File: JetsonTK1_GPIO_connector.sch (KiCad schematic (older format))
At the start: 35 parts

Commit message: アートワーク開始
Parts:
- removed P?: CONN_02X08, symbol CONN_02X08
- added JP2, JP3, JP6: Jumper_NC_Dual, Connect:GS3, symbol Jumper_NC_Dual
- added P4: CONN_01X01, Pin_Headers:Pin_Header_Straight_1x01, symbol CONN_01X01
- added P5, P6: CONN_01X04, Pin_Headers:Pin_Header_Straight_1x04, symbol CONN_01X04
- added P9: CONN_02X10, Pin_Headers:Pin_Header_Straight_2x10, symbol CONN_02X10
- added R10, R11, R13, R15, R17, R3, R4, R5, R6, R7, R8, R9: R, Resistors_SMD:R_0603, symbol R
- C1, C2, C3, C4, C5: renamed from C?; footprint (none) -> Capacitors_SMD:C_0603
- D1, D2, D3, D4: renamed from D?; footprint (none) -> LEDs:LED_0603
- JP1, JP4, JP5, JP7, JP8: renamed from JP?; footprint (none) -> Connect:GS3
- P1: renamed from P?; footprint (none) -> Pin_Headers:Pin_Header_Straight_1x25_Pitch2.00mm
- P10: renamed from P?; footprint (none) -> Pin_Headers:Pin_Header_Straight_1x10
- P2, P3: renamed from P?; footprint (none) -> Pin_Headers:Pin_Header_Straight_2x25_Pitch2.00mm
- P7, P8: renamed from P?; footprint (none) -> Pin_Headers:Pin_Header_Straight_1x04
- R1, R12, R14, R16, R18, R19, R2, R20, R21, R22, R23: renamed from R?; footprint (none) -> Resistors_SMD:R_0603
- gave numbers to parts that had none: 3
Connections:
- net +12V: now also P3.26 (P26); no longer P3.25 (P25)
- net +1V8: now also P3.20 (P20), P3.4 (P4), R11.1, R13.1, R3.1, R4.1, R5.1, R6.1; no longer C4.2, JP4.3, JP5.3, JP7.3, P3.19 (P19), P3.3 (P3), U2.24 (VDD)
- net +3V3: now also P3.15 (P15), JP2.1, JP3.1, JP6.1; no longer P3.16 (P16)
- net +5V: now also P2.2 (P2), P3.2 (P2), JP2.3, JP3.3, JP6.3; no longer P2.1 (P1), P3.1 (P1)
- net CAM_I2C_SCL: now also P2.7 (P7), R11.2; no longer P2.8 (P8)
- net CAM_I2C_SDA: now also P2.5 (P5), R13.2; no longer P2.6 (P6)
- net GEN1_I2C_SCL: now also P2.37 (P37), R3.2; no longer P2.38 (P38)
- net GEN1_I2C_SDA: now also P2.39 (P39), R5.2; no longer P2.40 (P40)
- net GND: now also P2.14 (P14), P2.15 (P15), P2.21 (P21), P2.25 (P25), P2.31 (P31), P2.41 (P41), P2.50 (P50), P2.8 (P8), P2.9 (P9), P3.1 (P1), P3.10 (P10), P3.13 (P13), P3.16 (P16), P3.25 (P25), P3.30 (P30), P3.31 (P31), P3.36 (P36), P3.37 (P37), P3.42 (P42), P3.43 (P43), P3.48 (P48), P3.7 (P7), P5.4 (P4), P6.4 (P4), P9.19 (P19), P9.20 (P20); no longer P2.10 (P10), P2.13 (P13), P2.16 (P16), P2.22 (P22), P2.26 (P26), P2.32 (P32), P2.42 (P42), P2.49 (P49), P2.7 (P7), P3.14 (P14), P3.15 (P15), P3.2 (P2), P3.26 (P26), P3.29 (P29), P3.32 (P32), P3.35 (P35), P3.38 (P38), P3.41 (P41), P3.44 (P44), P3.47 (P47), P3.8 (P8), P3.9 (P9)
- net GPIO_PH1: now also P3.49 (P49); no longer P3.50 (P50)
- net GPIO_PK2: now also P3.18 (P18); no longer P3.17 (P17)
- net GPIO_PU0: now also P2.28 (P28); no longer P2.27 (P27)
- net GPIO_PU1: now also P2.30 (P30); no longer P2.29 (P29)
- net GPIO_PU2: now also P2.32 (P32); no longer P2.31 (P31)
- net GPIO_PU3: now also P2.34 (P34); no longer P2.33 (P33)
- net GPIO_PU4: now also P2.36 (P36); no longer P2.35 (P35)
- net GPIO_PU5: now also P2.38 (P38); no longer P2.37 (P37)
- net GPIO_PU6: now also P2.40 (P40); no longer P2.39 (P39)
- net I2C_SCL_1V8: now also P3.22 (P22); no longer P3.21 (P21)
- net I2C_SCL_3V3: now also P3.17 (P17); no longer P3.18 (P18)
- net I2C_SDA_1V8: now also P3.24 (P24); no longer P3.23 (P23)
- net I2C_SDA_3V3: now also P3.19 (P19); no longer P3.20 (P20)
- net PWR_I2C_SCL: now also P2.33 (P33), R4.2; no longer P2.34 (P34)
- net PWR_I2C_SDA: now also P2.35 (P35), R6.2; no longer P2.36 (P36)
- net TS_SPI_CS_L: now also P3.5 (P5); no longer P3.6 (P6)
- net TS_SPI_MISO: now also P3.8 (P8); no longer P3.7 (P7)
- net TS_SPI_MOSI: now also P3.6 (P6); no longer P3.5 (P5)
- net TS_SPI_SCK: now also P3.3 (P3); no longer P3.4 (P4)
- net logic_conv_1/HV1: now also P5.2 (P2), R7.2
- net logic_conv_1/HV2: now also P5.3 (P3), R9.2
- net logic_conv_1/VH: now also JP2.2, P5.1 (P1), R7.1, R9.1
- net logic_conv_2/HV1: now also P6.2 (P2), R8.2
- net logic_conv_2/HV2: now also P6.3 (P3), R10.2
- net logic_conv_2/VH: now also JP3.2, P6.1 (P1), R10.1, R8.1
- net at U2.1 (~INT): now also P4.1 (P1)
- net at U2.10 (P0_6): now also P9.6 (P6)
- net at U2.11 (P0_7): now also P9.4 (P4)
- net at U2.13 (P1_0): now also P9.17 (P17)
- net at U2.14 (P1_1): now also P9.15 (P15)
- net at U2.15 (P1_2): now also P9.13 (P13)
- net at U2.16 (P1_3): now also P9.11 (P11)
- net at U2.17 (P1_4): now also P9.9 (P9)
- net at U2.18 (P1_5): now also P9.7 (P7)
- net at U2.19 (P1_6): now also P9.5 (P5)
- net at U2.20 (P1_7): now also P9.3 (P3)
- net logic_conv_3/HV1: now reaches U2.22 (SCL)
- net logic_conv_3/HV1: now also R15.2
- net logic_conv_3/HV2: now reaches U2.23 (SDA)
- net logic_conv_3/HV2: now also R17.2
- net at U2.4 (P0_0): now also P9.18 (P18)
- net at U2.5 (P0_1): now also P9.16 (P16)
- net at U2.6 (P0_2): now also P9.14 (P14)
- net at U2.7 (P0_3): now also P9.12 (P12)
- net at U2.8 (P0_4): now also P9.10 (P10)
- net at U2.9 (P0_5): now also P9.8 (P8)
- new net logic_conv_3/VH: C4.2, JP4.3, JP5.3, JP6.2, JP7.3, P9.1 (P1), P9.2 (P2), R15.1, R17.1, U2.24 (VDD)
- no-connect marks 2 -> 74
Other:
- moved on the sheet: C4, JP4, JP5, JP7, P8, R18, R19, U2

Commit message: 進捗
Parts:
- removed R10, R11, R13, R15, R17, R3, R4, R5, R6, R7, R8, R9: R, Resistors_SMD:R_0603, symbol R
- P10: footprint Pin_Headers:Pin_Header_Straight_1x10 -> Connectors_JST:JST_XH_B10B-XH-A_10x2.50mm_Straight
- P5, P6, P7, P8: footprint Pin_Headers:Pin_Header_Straight_1x04 -> Connectors_JST:JST_XH_B04B-XH-A_04x2.50mm_Straight
- P9: footprint Pin_Headers:Pin_Header_Straight_2x10 -> Connect:IDC_Header_Straight_20pins
- renumbered R22 to R10, R23 to R11, R12 to R3, R14 to R4, R16 to R5, R18 to R6, R19 to R7, R20 to R8, R21 to R9
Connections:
- net GPIO_PH1: now also U3.9 (A8); no longer U3.1 (A1)
- net GPIO_PU0: now also U3.1 (A1); no longer U3.3 (A2)
- net GPIO_PU1: now also U3.3 (A2); no longer U3.4 (A3)
- net GPIO_PU2: now also U3.4 (A3); no longer U3.5 (A4)
- net GPIO_PU3: now also U3.5 (A4); no longer U3.6 (A5)
- net GPIO_PU4: now also U3.6 (A5); no longer U3.7 (A6)
- net GPIO_PU5: now also U3.7 (A6); no longer U3.8 (A7)
- net GPIO_PU6: now also U3.8 (A7); no longer U3.9 (A8)

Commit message: ver1.0完成，これでElecrow発注
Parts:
- P9: footprint Connect:IDC_Header_Straight_20pins -> Connectors_Multicomp:Multicomp_MC9A12-2034_2x10x2.54mm_Straight
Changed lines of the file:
@@
 EESchema Schematic File Version 2
+LIBS:JetsonTK1_GPIO_connector-rescue
 LIBS:power
 LIBS:device
@@
 F 0 "P9" H 10200 2900 50  0000 C CNN
 F 1 "CONN_02X10" V 10200 2350 50  0000 C CNN
-F 2 "Connect:IDC_Header_Straight_20pins" H 10200 1150 50  0001 C CNN
+F 2 "Connectors_Multicomp:Multicomp_MC9A12-2034_2x10x2.54mm_Straight" H 10200 1150 50  0001 C CNN
 F 3 "" H 10200 1150 50  0000 C CNN
 	1    10200 2350

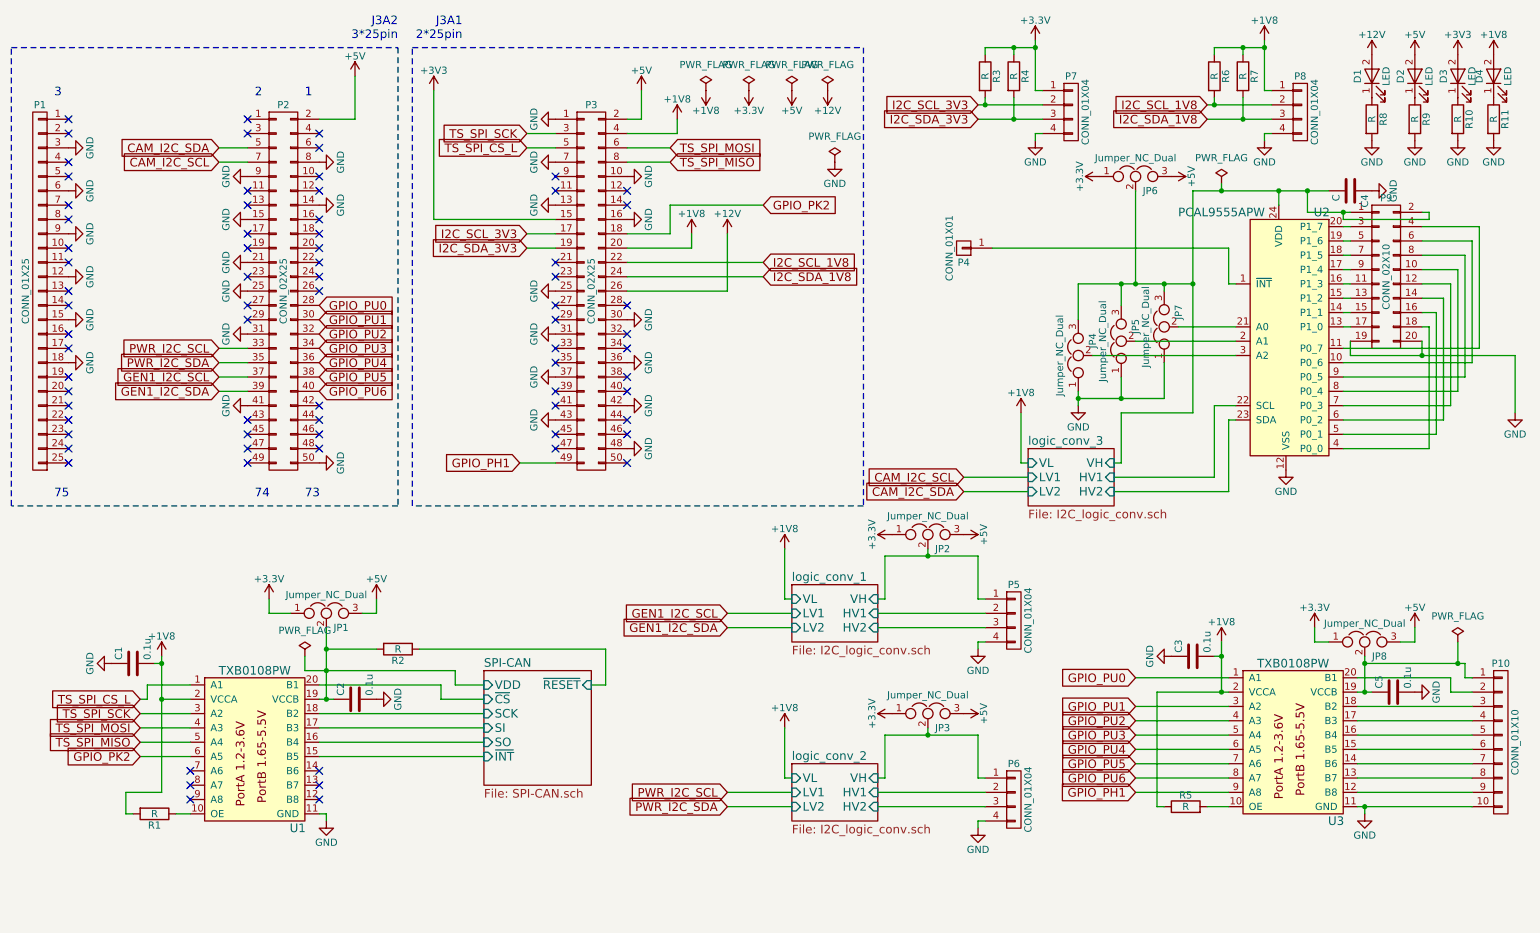
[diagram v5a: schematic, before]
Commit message: 部品に定数を追加
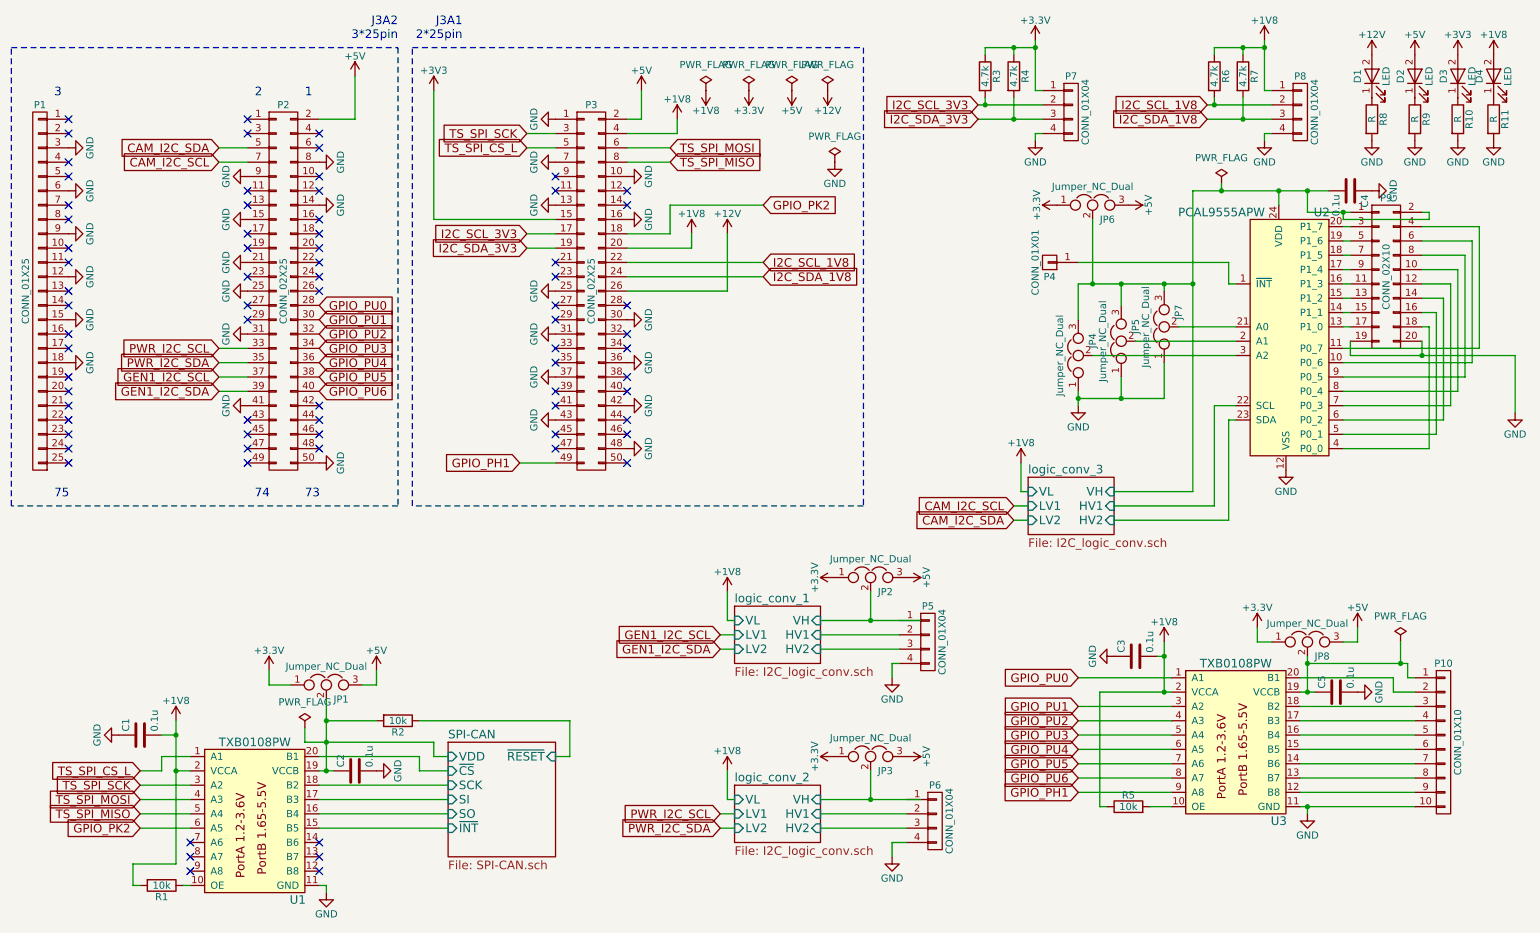
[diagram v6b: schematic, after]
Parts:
- C4: value C -> 0.1u
- R1, R2, R5: value R -> 10k
- R3, R4, R6, R7: value R -> 4.7k
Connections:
- net logic_conv_1/VH: no longer P5.1 (P1)
- net logic_conv_2/VH: no longer P6.1 (P1)
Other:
- moved on the sheet: C1, C2, C3, C5, JP1, JP2, JP3, JP6, JP8, P10, P4, P5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
